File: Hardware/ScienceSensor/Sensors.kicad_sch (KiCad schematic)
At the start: 58 parts, among them J1 USB_A, Q10 BSS138, Q2 BSS138, Q4 BSS138, Q6 BSS138, Q7 BSS138, Q8 BSS138, Q9 BSS138, U4 FT230XS, U5 TSV911RILT, U6 TSV911RILT

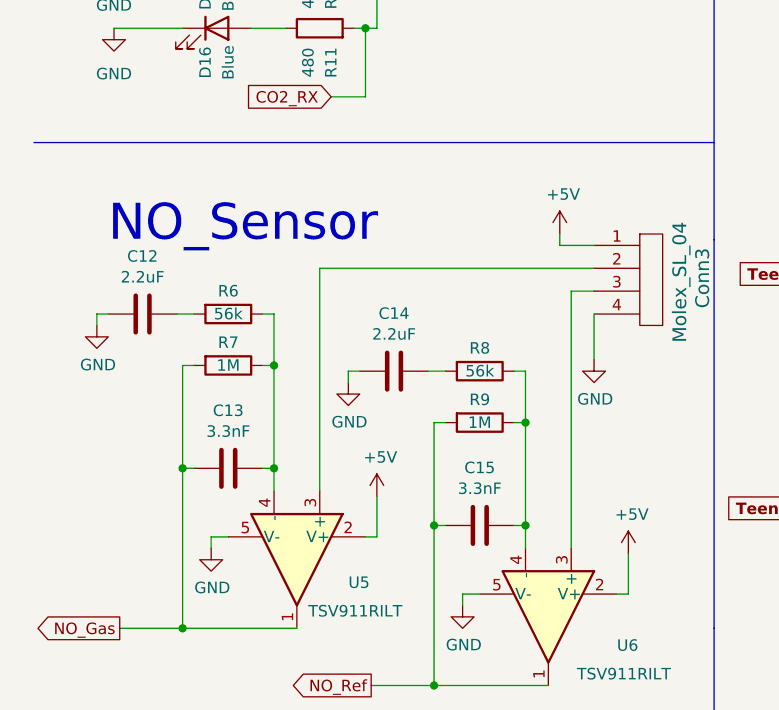
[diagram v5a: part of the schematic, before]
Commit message: Changed NO molex to match others
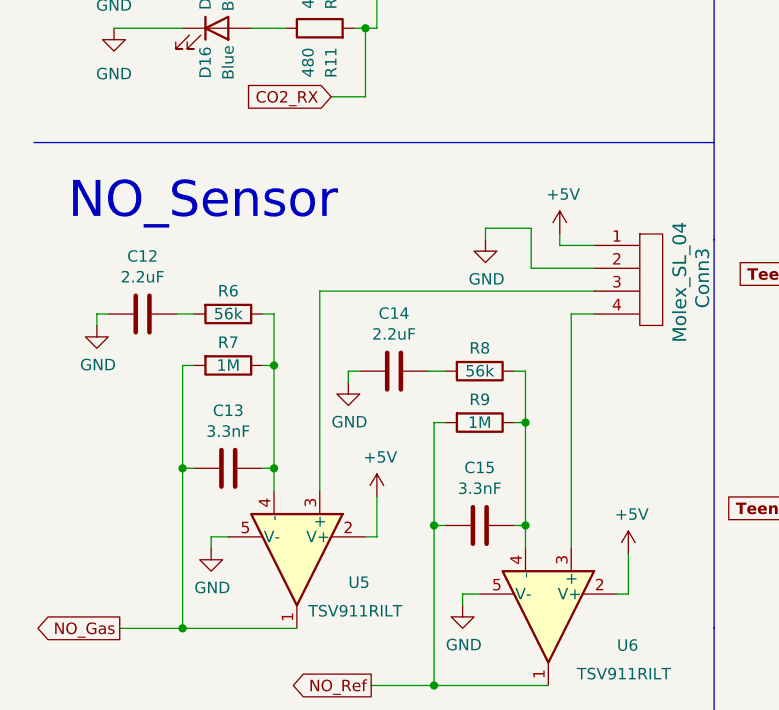
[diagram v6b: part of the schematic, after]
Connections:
- net GND: now also Conn3.2; no longer Conn3.4
- net at U5.3 (+): now also Conn3.3; no longer Conn3.2
- net at U6.3 (+): now also Conn3.4; no longer Conn3.3
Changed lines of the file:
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@@
     (stroke (width 0) (type default) (color 0 0 0 0))
   )
-  (wire (pts (xy 71.755 111.125) (xy 71.755 139.7))
-    (stroke (width 0) (type default) (color 0 0 0 0))
-  )
-  (wire (pts (xy 74.295 108.585) (xy 43.815 108.585))
+  (wire (pts (xy 74.295 111.125) (xy 43.815 111.125))
     (stroke (width 0) (type default) (color 0 0 0 0))
   )
@@
     (stroke (width 0) (type default) (color 0 0 0 0))
   )
-  (wire (pts (xy 74.295 113.665) (xy 74.295 118.745))
+  (wire (pts (xy 67.31 104.14) (xy 62.23 104.14))
     (stroke (width 0) (type default) (color 0 0 0 0))
   )
@@
     (stroke (width 0) (type default) (color 0 0 0 0))
   )
+  (wire (pts (xy 71.755 113.665) (xy 71.755 139.7))
+    (stroke (width 0) (type default) (color 0 0 0 0))
+  )
   (wire (pts (xy 142.24 64.77) (xy 142.24 66.04))
     (stroke (width 0) (type default) (color 0 0 0 0))
@@
     (stroke (width 0) (type default) (color 0 0 0 0))
   )
+  (wire (pts (xy 67.31 108.585) (xy 74.295 108.585))
+    (stroke (width 0) (type default) (color 0 0 0 0))
+  )
   (wire (pts (xy 137.16 64.77) (xy 142.24 64.77))
     (stroke (width 0) (type default) (color 0 0 0 0))
@@
     (stroke (width 0) (type default) (color 0 0 0 0))
   )
-  (wire (pts (xy 43.815 108.585) (xy 43.815 133.35))
-    (stroke (width 0) (type default) (color 0 0 0 0))
-  )
   (wire (pts (xy 56.515 19.685) (xy 56.515 17.78))
     (stroke (width 0) (type default) (color 0 0 0 0))
@@
     (stroke (width 0) (type default) (color 0 0 0 0))
   )
+  (wire (pts (xy 62.23 104.14) (xy 62.23 105.41))
+    (stroke (width 0) (type default) (color 0 0 0 0))
+  )
   (wire (pts (xy 180.34 101.6) (xy 180.34 96.52))
     (stroke (width 0) (type default) (color 0 0 0 0))
@@
     (stroke (width 0) (type default) (color 0 0 0 0))
   )
-  (wire (pts (xy 74.295 111.125) (xy 71.755 111.125))
+  (wire (pts (xy 74.295 113.665) (xy 71.755 113.665))
     (stroke (width 0) (type default) (color 0 0 0 0))
   )
@@
     (stroke (width 0) (type default) (color 0 0 0 0))
   )
+  (wire (pts (xy 43.815 111.125) (xy 43.815 133.35))
+    (stroke (width 0) (type default) (color 0 0 0 0))
+  )
   (wire (pts (xy 121.92 40.64) (xy 121.92 29.21))
     (stroke (width 0) (type default) (color 0 0 0 0))
@@
   )
   (wire (pts (xy 137.16 45.72) (xy 152.4 45.72))
+    (stroke (width 0) (type default) (color 0 0 0 0))
+  )
+  (wire (pts (xy 67.31 104.14) (xy 67.31 108.585))
     (stroke (width 0) (type default) (color 0 0 0 0))
   )
@@
     (effects (font (size 4 4)) (justify left bottom))
   )
-  (text "NO_Sensor" (at 20.32 106.045 0)
+  (text "NO_Sensor" (at 15.875 103.505 0)
     (effects (font (size 4 4)) (justify left bottom))
   )
@@
     (pin "2")
   )
-  (symbol (lib_id "power:GND") (at 74.295 118.745 0) (unit 1)
-    (in_bom yes) (on_board yes)
-    (property "Reference" "#PWR0103" (id 0) (at 74.295 125.095 0)
-      (effects (font (size 1.27 1.27)) hide)
-    )
-    (property "Value" "GND" (id 1) (at 74.422 123.1392 0))
-    (property "Footprint" "" (id 2) (at 74.295 118.745 0)
-      (effects (font (size 1.27 1.27)) hide)
-    )
-    (property "Datasheet" "" (id 3) (at 74.295 118.745 0)
-      (effects (font (size 1.27 1.27)) hide)
-    )
+  (symbol (lib_id "power:GND") (at 62.23 105.41 0) (unit 1)
+    (in_bom yes) (on_board yes)
+    (property "Reference" "#PWR0103" (id 0) (at 62.23 111.76 0)
+      (effects (font (size 1.27 1.27)) hide)
+    )
+    (property "Value" "GND" (id 1) (at 62.357 109.8042 0))
+    (property "Footprint" "" (id 2) (at 62.23 105.41 0)
+      (effects (font (size 1.27 1.27)) hide)
+    )
+    (property "Datasheet" "" (id 3) (at 62.23 105.41 0)
+      (effects (font (size 1.27 1.27)) hide)
+    )

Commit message: Schematic Review
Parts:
- removed C10, C6: 100nF, symbol Device:C
- removed C5: 10nF, symbol Device:C
- removed C7: 4.7, symbol Device:C_Polarized_US
- removed C8, C9: 47pF, symbol Device:C
- removed D17, D18: Blue, symbol Device:LED
- removed FB1: Ferrite_Bead, symbol Device:FerriteBead
- removed J1: USB_A, symbol Connector:USB_A
- removed R20, R21: 27, symbol Device:R
- removed R28, R29: 480, symbol Device:R
- removed U4: FT230XS, Package_SO:SSOP-16_3.9x4.9mm_P0.635mm, symbol Interface_USB:FT230XS
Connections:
- no-connect marks 6 -> 0
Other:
- note removed: "Methane Sensor"
- note removed: "This can probably be removed"
- note removed: "USB Port"
- note removed: "USB to UART Converter"
